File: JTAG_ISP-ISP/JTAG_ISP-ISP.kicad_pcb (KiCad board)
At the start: 2 copper layers, 23.1 x 46.1 mm, 11 parts, among them J1 Conn_02x03_Odd_Even, J2 Conn_01x08, J3 Conn_01x08

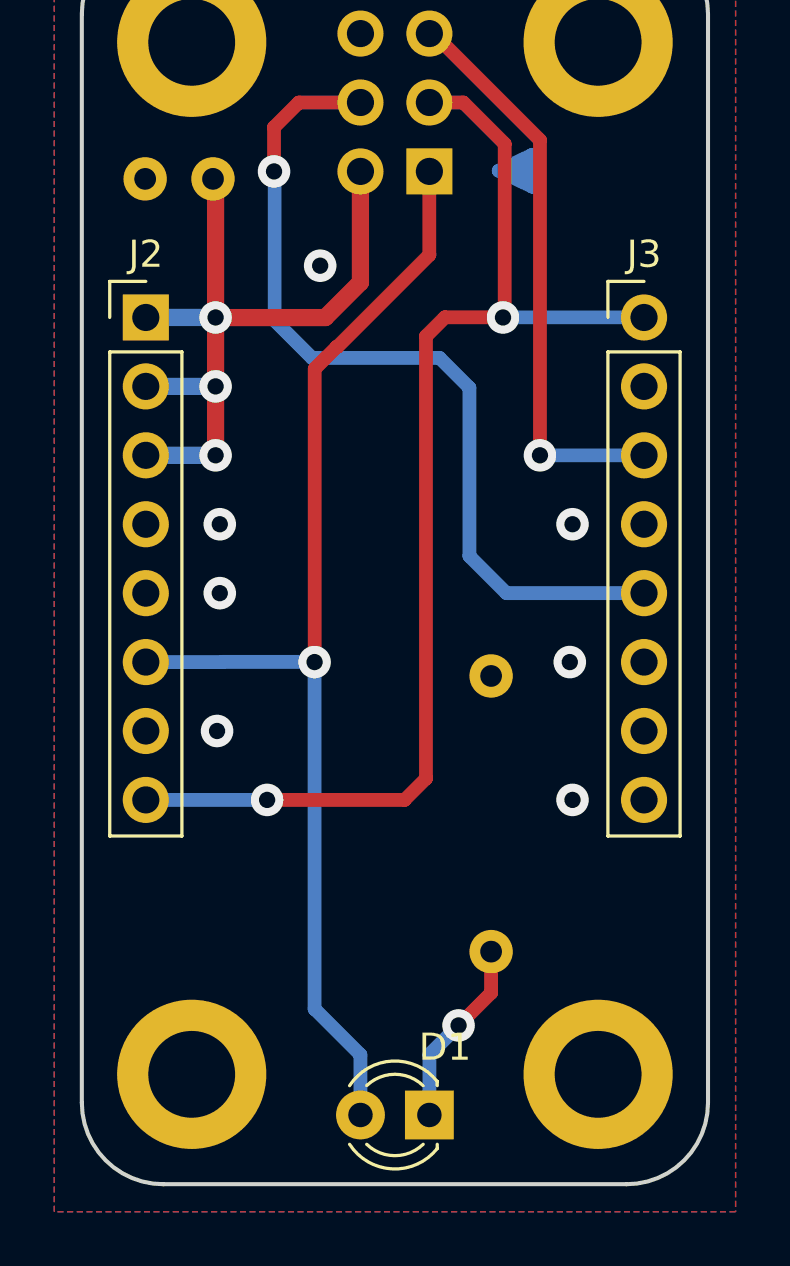
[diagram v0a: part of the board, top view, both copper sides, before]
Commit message: # Version compacte en cours... ## Les headers passent à travers d'un PCB et dépassent moins que la version précédente.
# [PCB]
+ Ajout d'un trou pour l'ISP dans le PCB du projet HDR.
+ Ajout d'un trou pour le PICkit dans le PCB du projet ISP.
* Déplacement du circuit de DEL dans le projet HDR.
* Projet ISP routé à nouveau.
* Mise à jour de la cartouche pour les 2 projets.
    * Date actuelle;
    * Version actuelle;

# [SCHÉMA]
+ Ajout d'encadrés pointillés dan les 2 projets pour séparer les parties du schémas.
* Déplacement du circuit de DEL dans le projet HDR.
* Réduction de la valeur de la résistance pour le circuit de DEL.
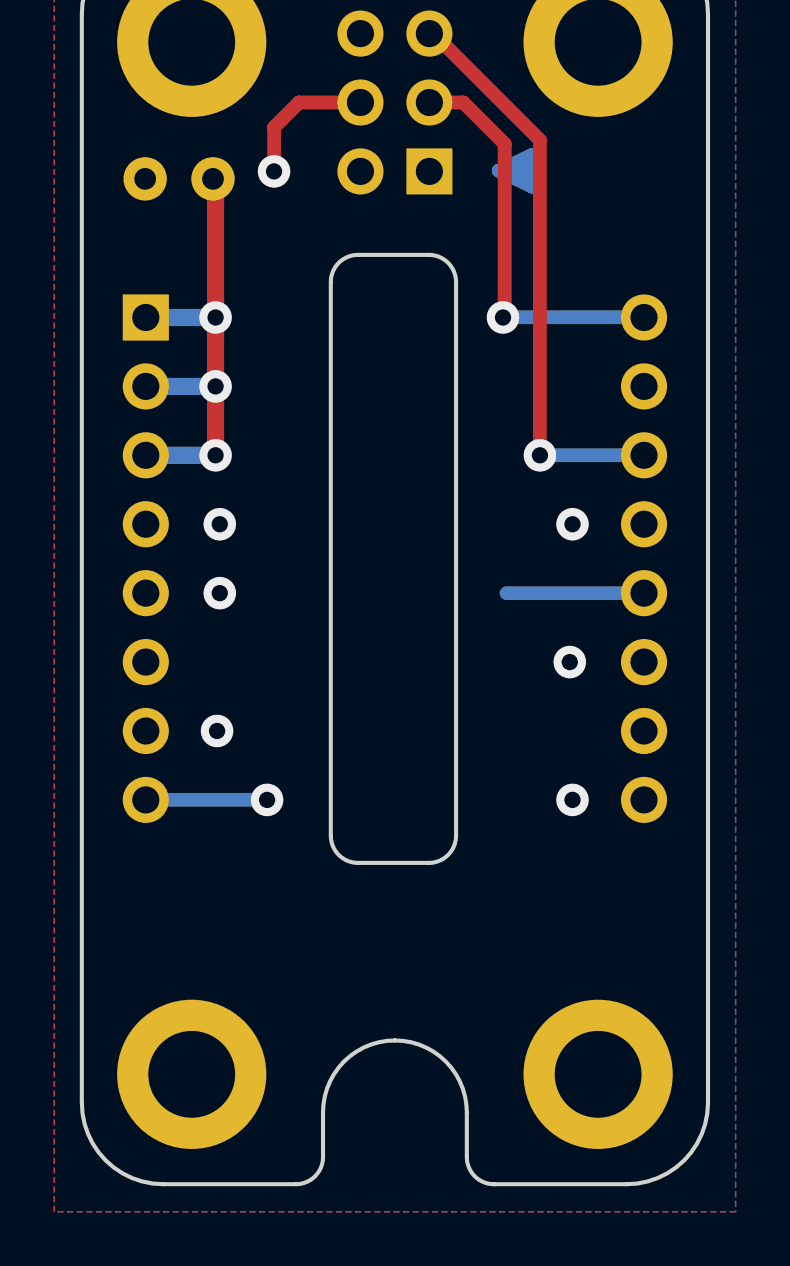
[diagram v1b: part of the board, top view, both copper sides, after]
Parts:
- removed D1: LED, LED_THT:LED_D3.0mm
- removed R1: 2k, Resistor_THT:R_Axial_DIN0207_L6.3mm_D2.5mm_P10.16mm_Horizontal
- J2, J3: moved to B.Cu
- turned J2 to 180 degrees
- turned J3 to 180 degrees
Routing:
- net MISO: track 43.5 -> 0.00 mm, vias 1 -> 0
- net SCLK: track 45.1 -> 19.5 mm
- net MOSI: track 32.1 -> 10.2 mm
- net +5V: track 28.1 -> 18.1 mm
- net Net-(D1-Pad1): track 6.96 -> 0.00 mm, vias 1 -> 0
- net GND: vias 7 -> 6
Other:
- outline, holes or cut-outs redrawn

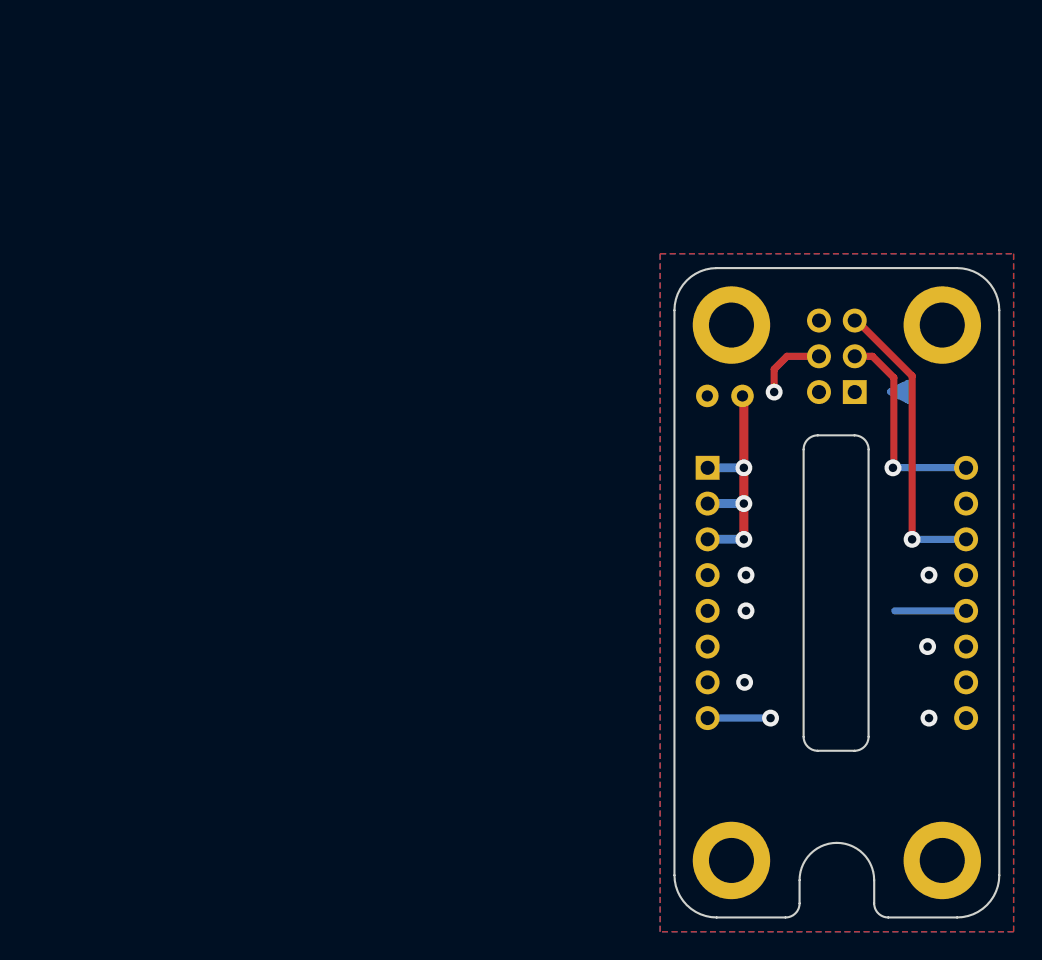
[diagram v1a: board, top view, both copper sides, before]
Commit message: # [PCB] + Ajout du dégagement de 40 mils sur la bordure du trou au centre du PCB et sur le pourtour. [ISP] + Ajout du texte (date du jour) dans le bas du PCB. [ISP] + Ajout de la flèche indiquand la broche #1 du header PICkit4. [ISP] + Double vias pour les traces d'alimentation. - Suppression de la flèche indiquand la broche #1 du header ISP. [ISP] * Nouveau format de page A5. * PCB routé à nouveau. [ISP] * Mise à jour de la cartouche. [ISP]     * Date actuelle;
# [SCHÉMA]
* Mise à jour de la cartouche. [ISP]
    * Date actuelle.
* Nouveau format de page A5.
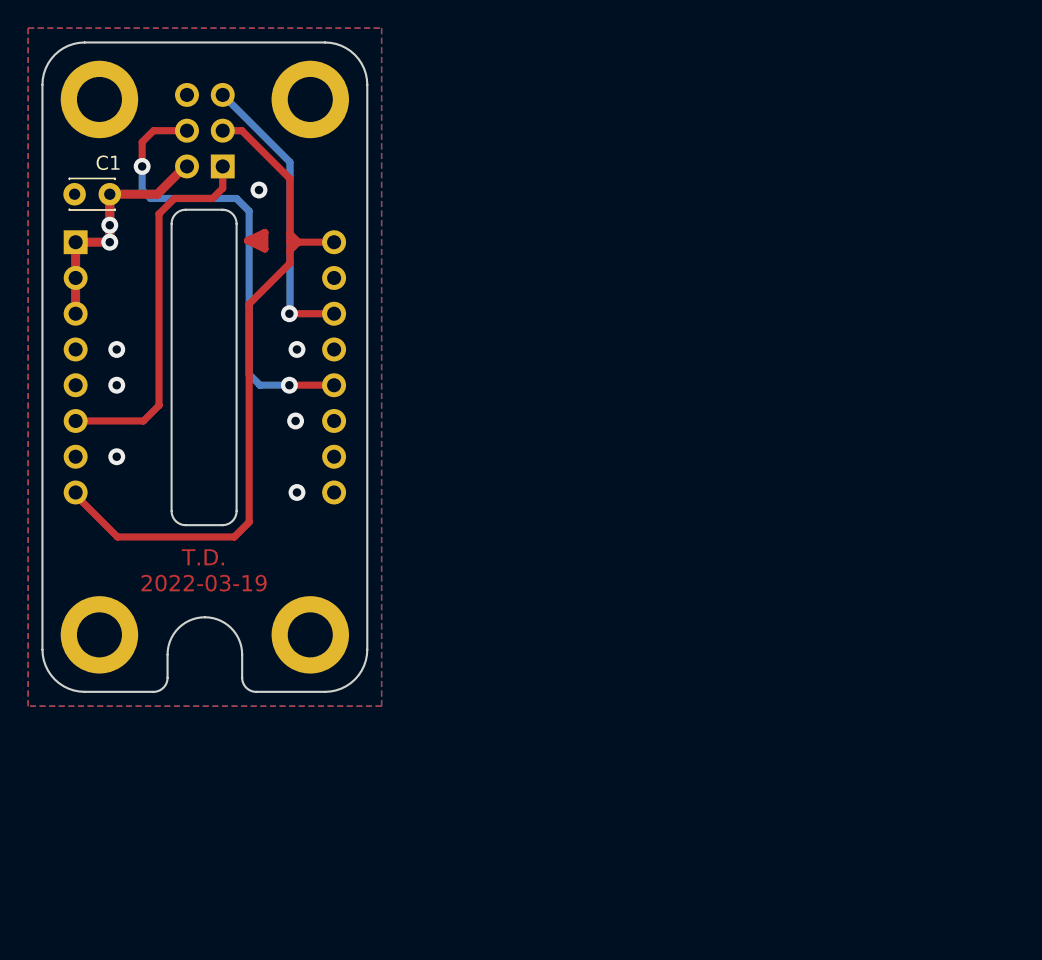
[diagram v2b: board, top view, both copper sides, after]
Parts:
- C1, REF**: moved to F.Cu
- moved REF** 47.7 mm to (104.0, 49.3)
- moved REF** 47.7 mm to (104.0, 87.4)
- moved J2 47.7 mm to (102.3, 59.5)
- moved J3 47.7 mm to (120.6, 59.5)
- moved J1 47.7 mm to (112.7, 54.1)
- moved REF** 47.7 mm to (119.0, 49.3)
- moved REF** 47.7 mm to (119.0, 87.4)
- moved C1 47.2 mm to (104.7, 56.1)
- moved REF** 47.1 mm to (115.7, 59.0)
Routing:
- net SCLK: track 19.5 -> 50.8 mm, vias 2 -> 0
- net MISO: track 0.00 -> 26.8 mm
- net MOSI: track 10.2 -> 33.1 mm, vias 1 -> 2
- net +5V: track 18.1 -> 20.1 mm, vias 3 -> 2
- net GND: vias 6 -> 7
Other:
- board text added: "T.D. 2022-03-19"

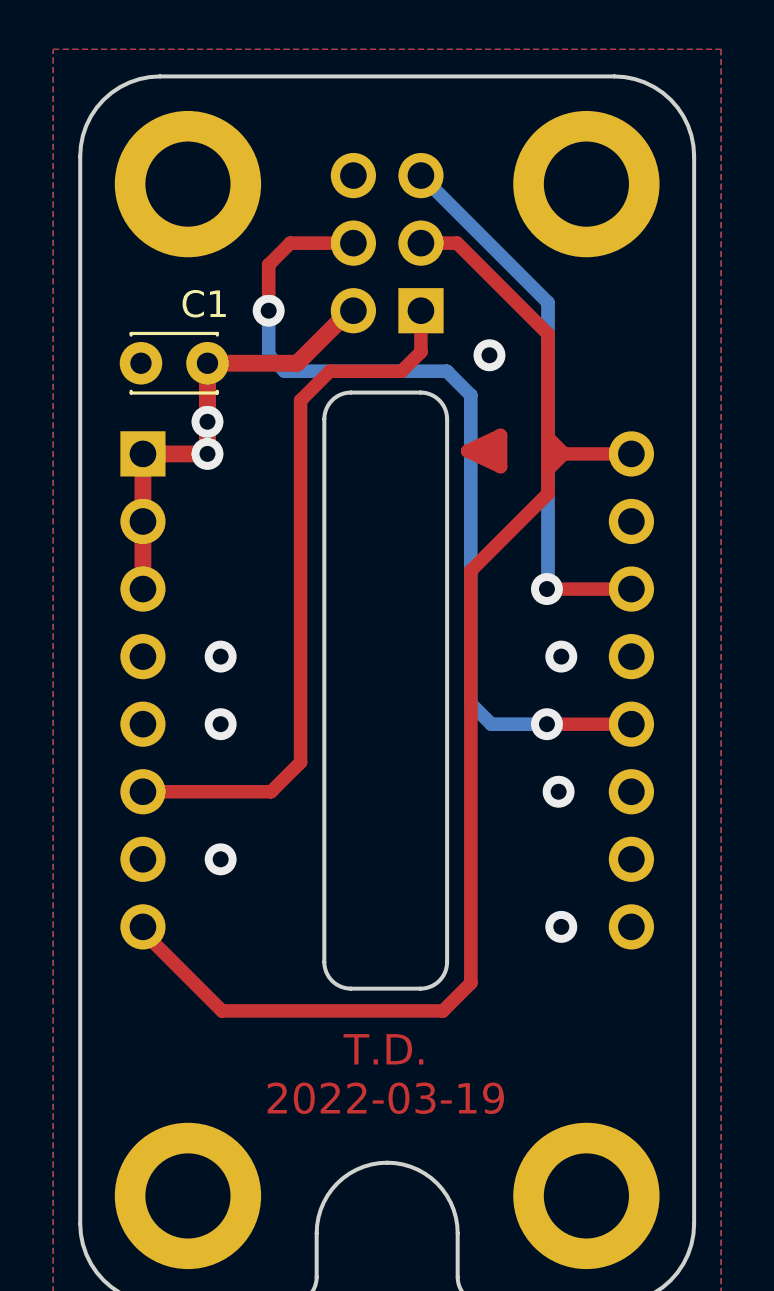
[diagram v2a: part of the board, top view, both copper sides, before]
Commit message: # [PCB] + Ajout de vias pour assurer la bonne connexion du ground. [ISP] * Correction trace RESET sur mauvaise couche. [ISP] * Modification du texte. [ISP]     * Date du jour;     + Version actuelle. * Mise à jour de la cartouche. [ISP]     * Date actuelle;     * Version actuelle.
# [SCHÉMA]
* Mise à jour de la cartouche. [ISP]
    * Date actuelle;
    * Version actuelle.
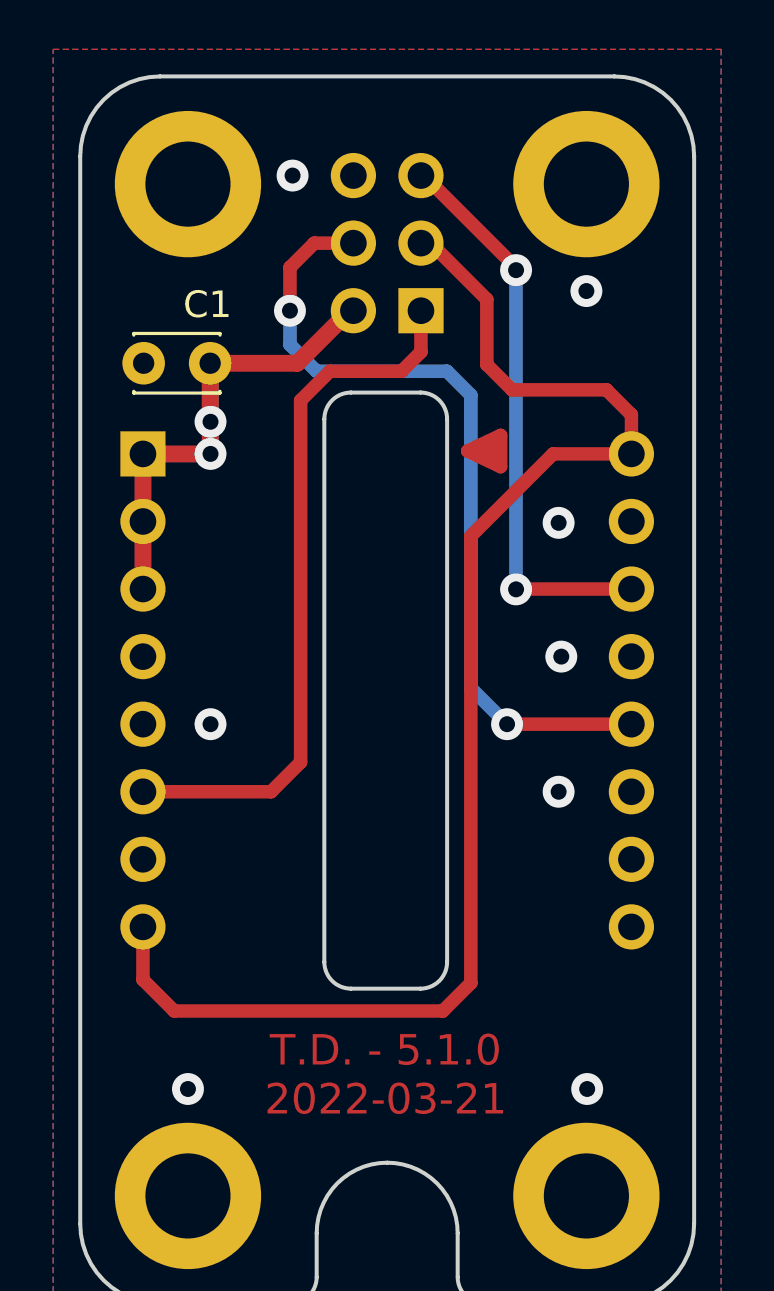
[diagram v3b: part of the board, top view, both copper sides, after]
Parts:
- moved C1 0.10 mm to (104.8, 56.1)
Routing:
- net MOSI: track 33.1 -> 30.9 mm
- net SCLK: track 50.8 -> 52.8 mm
- net +5V: track 20.1 -> 20.9 mm
- net RESET: track 20.7 -> 21.4 mm, vias 1 -> 2
- net GND: track 0.00 -> 0.04 mm, vias 7 -> 8
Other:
- board text added: "T.D. - 5.1.0 2022-03-21"
- board text removed: "T.D. 2022-03-19"

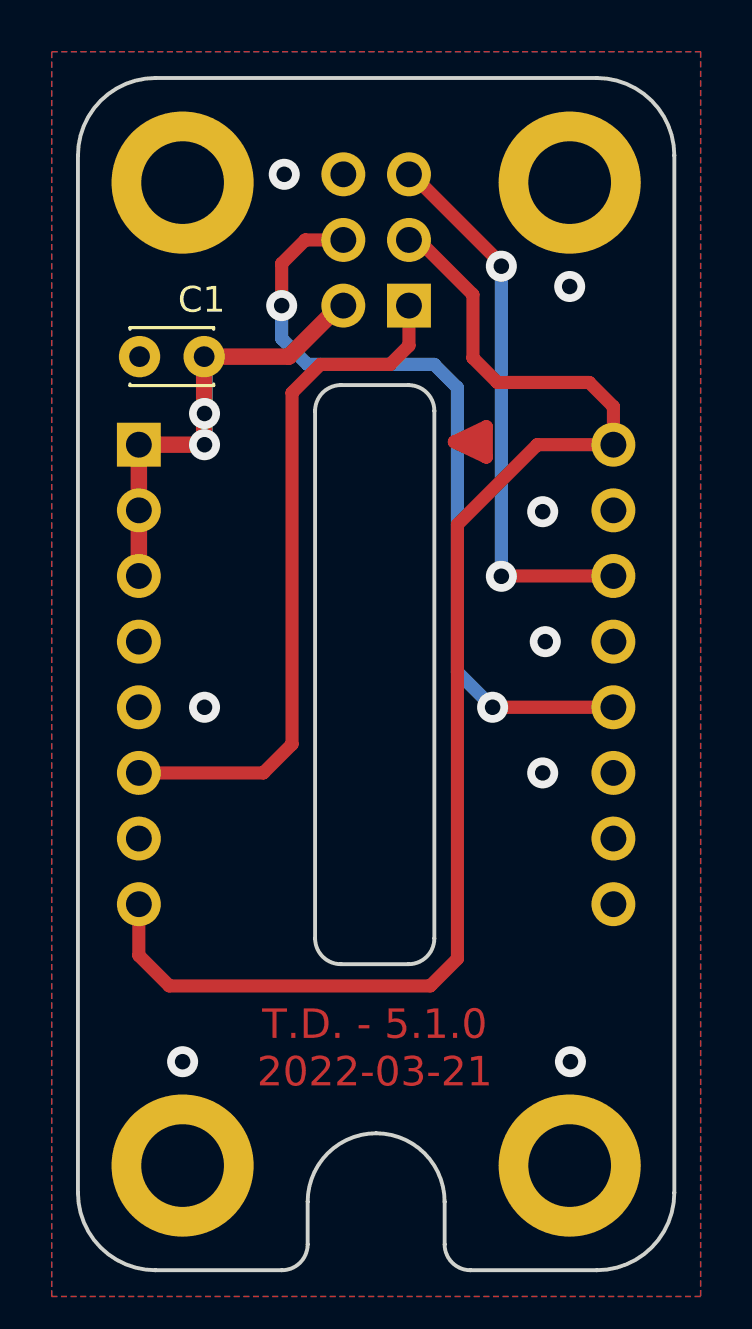
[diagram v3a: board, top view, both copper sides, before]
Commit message: # [PCB] + Ajout de vias pour le ground. + Routage du ground. * Mise à jour de la cartouche.     * Date actuelle;     * Version actuelle.
# [SCHÉMA]
* Mise à jour de la cartouche.
    * Date actuelle;
    * Version actuelle.
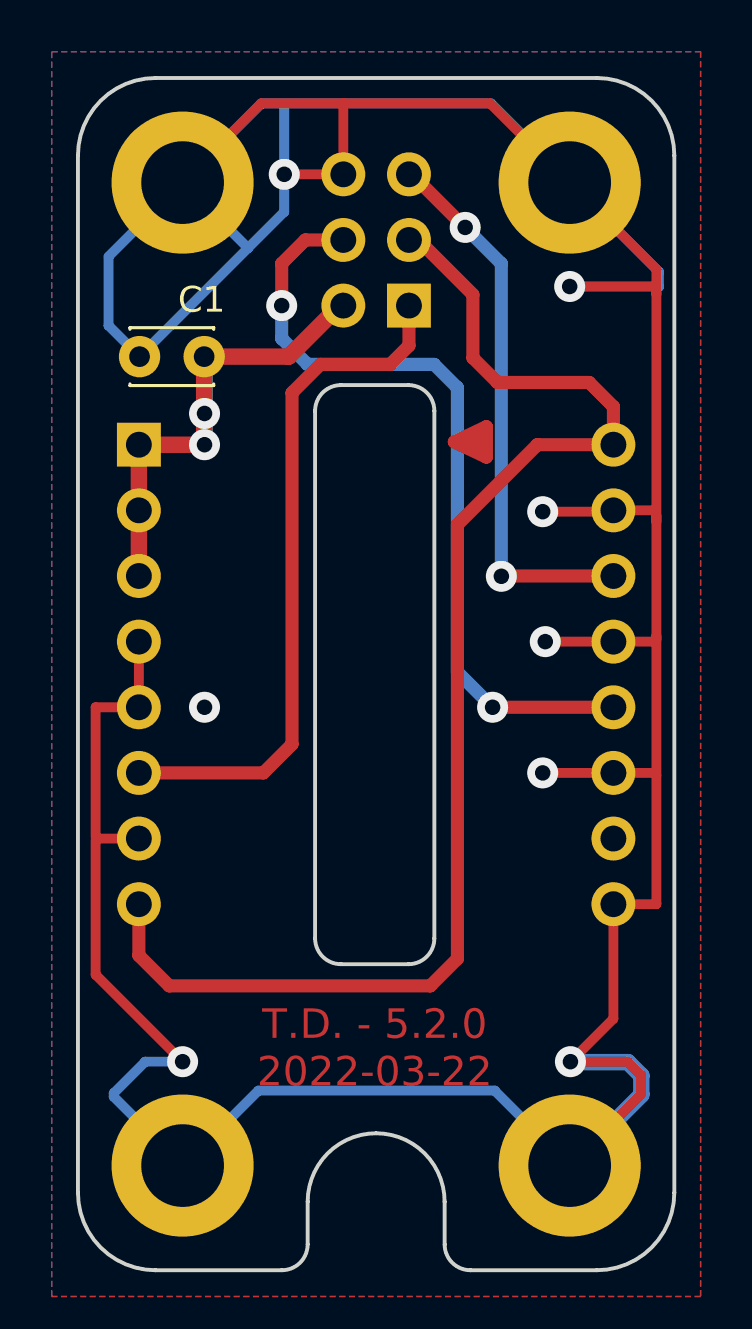
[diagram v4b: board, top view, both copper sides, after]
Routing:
- net GND: track 0.04 -> 188.1 mm
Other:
- board text added: "T.D. - 5.2.0 2022-03-22"
- board text removed: "T.D. - 5.1.0 2022-03-21"
